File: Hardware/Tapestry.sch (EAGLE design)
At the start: 120 parts, among them J1 CORTEX_DEBUGPTH, J10 3.3V, J11 VIN, J12 A4, J13 A5, J2 POWER_JACKPTH_LOCK, J3 AOUT4L, J4 AOUT4R, J5 AOUT5L, J6 AOUT5R, J7 AIN3R, J8 AIN3L, J9 3.3VA, U1 ATSAMS70NXXA-AN, U2 AK4618VQSFE-PACKAGE, U3 LM1117, U4 LM1117, Y1 12MHz

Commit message: Adding PROD IDs to components.
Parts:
- C7: device SparkFun-Capacitors:CAP0603-CAP -> SparkFun-Capacitors:10UF-6.3V-20%(0603)
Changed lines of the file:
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@@
 <part name="GND6" library="SparkFun-Aesthetics" deviceset="GND" device=""/>
 <part name="GND7" library="SparkFun-Aesthetics" deviceset="GND" device=""/>
-<part name="C7" library="SparkFun-Capacitors" deviceset="CAP" device="0603-CAP" value="10uF"/>
+<part name="C7" library="SparkFun-Capacitors" deviceset="10UF-6.3V-20%(0603)" device="" value="10uF"/>
 <part name="GND8" library="SparkFun-Aesthetics" deviceset="GND" device=""/>
 <part name="D3" library="SparkFun-DiscreteSemi" deviceset="DIODE-SCHOTTKY" device="-MBRA140" value="MBRA140"/>

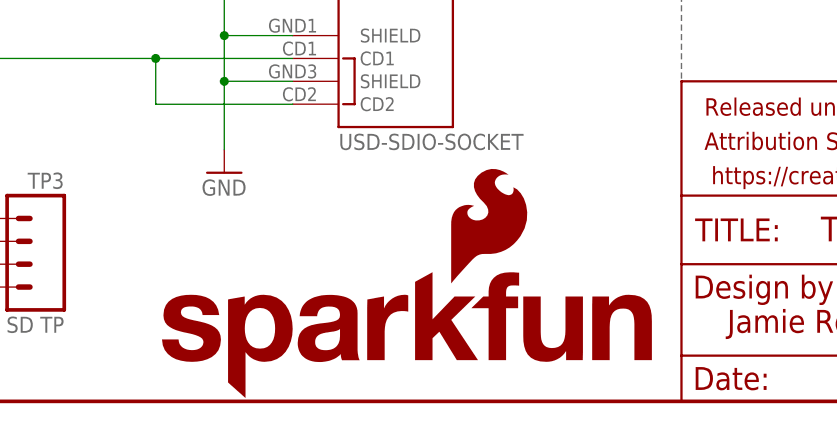
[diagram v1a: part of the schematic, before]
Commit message: Swapped location of SD socket and reset switches.
Added some more branding to silkscreen.
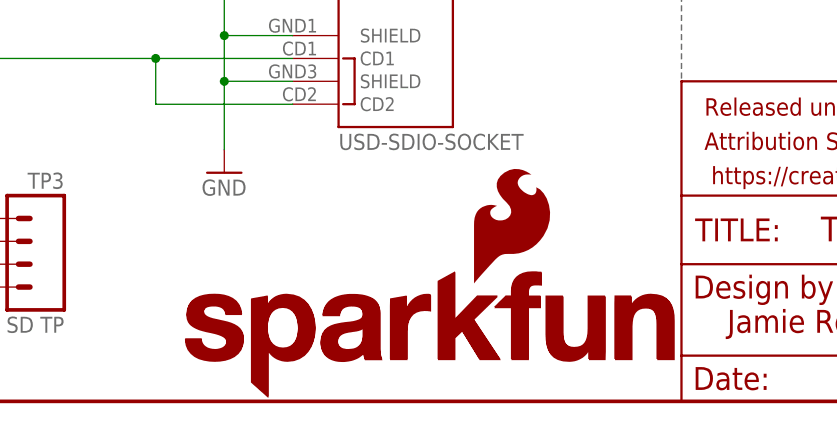
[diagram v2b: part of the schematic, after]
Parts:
- added LOGO3: SFE_LOGO_NAME.2_INCH, SparkFun-Aesthetics:SFE_LOGO_NAME.2_INCH
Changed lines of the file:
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@@
 <part name="GND45" library="SparkFun-Aesthetics" deviceset="GND" device=""/>
 <part name="LOGO2" library="SparkFun-Aesthetics" deviceset="OSHW-LOGO" device="M"/>
+<part name="LOGO3" library="SparkFun-Aesthetics" deviceset="SFE_LOGO_NAME" device=".2_INCH"/>
 </parts>
 <sheets>
@@
 <instance part="R25" gate="G$1" x="96.52" y="149.86" rot="R90"/>
 <instance part="R26" gate="G$1" x="104.14" y="149.86" rot="R90"/>
-<instance part="LOGO1" gate="G$1" x="271.78" y="0"/>
+<instance part="LOGO1" gate="G$1" x="274.32" y="0"/>
 <instance part="J2" gate="G$1" x="15.24" y="248.92"/>
 <instance part="GND43" gate="1" x="20.32" y="243.84"/>
@@
 <instance part="GND45" gate="1" x="347.98" y="215.9"/>
 <instance part="LOGO2" gate="G$1" x="419.1" y="45.72"/>
+<instance part="LOGO3" gate="G$1" x="273.05" y="0.508"/>
 </instances>
 <busses>

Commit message: Revising power input.
Using RG Keen's "ideal diode" for barrel input, avoiding a diode drop on
the barrel input, so it's prioritized over Vusb if both are plugged in.
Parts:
- removed D3, D4: MBRA140, SparkFun-DiscreteSemi:DIODE-SCHOTTKY-MBRA140
- added D2: MBRA140, SparkFun-DiscreteSemi:DIODE-SCHOTTKY-MBRA140
- added Q1: 2.5A/30V, SparkFun-DiscreteSemi:MOSFET-PCHANNELDMG2307L
- added R29: 1M, SparkFun-Resistors:1MOHM-1/10W-1%(0603)
- J2: value POWER_JACKPTH_LOCK -> POWER_JACK
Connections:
- new net N$75: Q1.G, R29.2
- net GND: now also R29.1
- net N$7: now also D2.A; no longer D3.A
- net N$9: now also D2.C, Q1.S; no longer D3.C, D4.C
- net VIN: now also Q1.D; no longer D4.A
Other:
- note added: "Power inputs prioritize barrel over USB. If 5V is present on both, current is drawn from barrel."
- moved on the sheet: C10, C11, C47, C8, C9, J10, J11, J2, J9, R18, R19, R20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

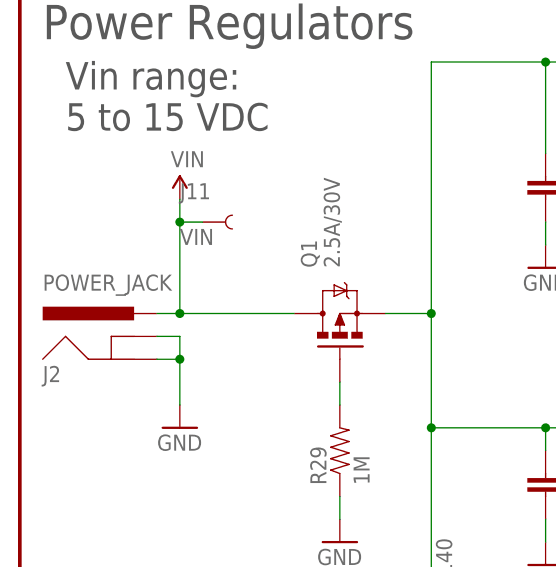
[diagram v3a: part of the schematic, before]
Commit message: Adding DNS designation to barrel jack.
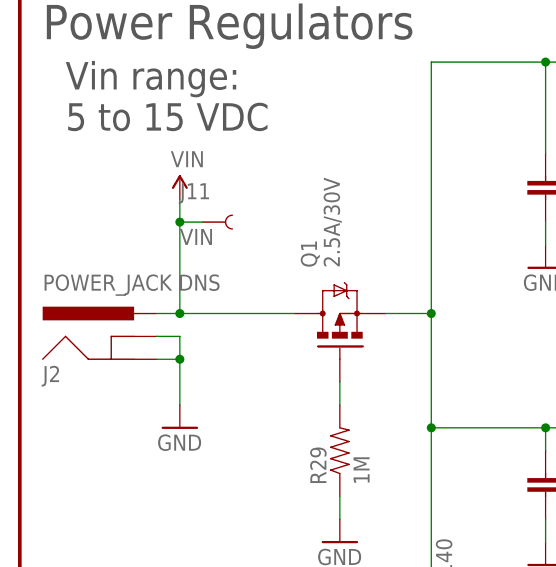
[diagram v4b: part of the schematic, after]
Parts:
- J2: value POWER_JACK -> POWER_JACK DNS
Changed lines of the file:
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@@
 <part name="R26" library="SparkFun-Resistors" deviceset="4.7KOHM-1/10W-1%(0603)" device="" value="4.7K"/>
 <part name="LOGO1" library="SparkFun-Aesthetics" deviceset="SFE_LOGO_NAME_FLAME" device=".2_INCH"/>
-<part name="J2" library="SparkFun-Connectors" deviceset="POWER_JACK" device="PTH_LOCK" value="POWER_JACK"/>
+<part name="J2" library="SparkFun-Connectors" deviceset="POWER_JACK" device="PTH_LOCK" value="POWER_JACK DNS"/>
 <part name="GND43" library="SparkFun-Aesthetics" deviceset="GND" device=""/>
 <part name="S2" library="SparkFun-Electromechanical" deviceset="SWITCH-MOMENTARY-2" device="SIDE_EZ" value="DNS"/>
